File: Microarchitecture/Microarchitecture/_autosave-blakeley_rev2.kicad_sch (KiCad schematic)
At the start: 15 parts

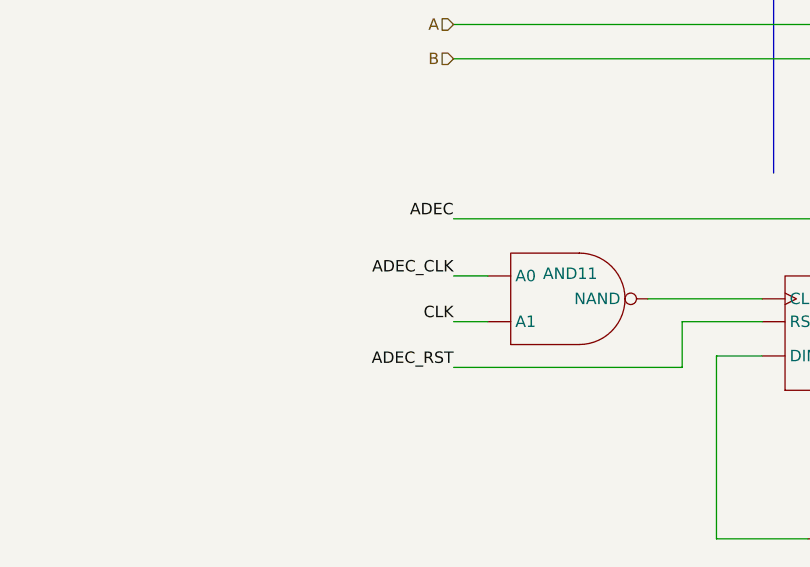
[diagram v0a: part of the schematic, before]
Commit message: Blakeley datapath working
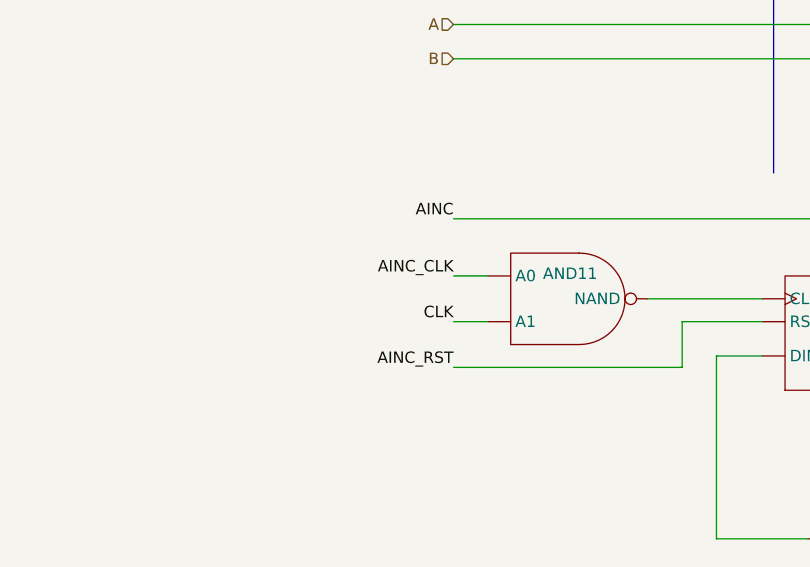
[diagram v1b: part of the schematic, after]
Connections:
- net ADEC_CLK is gone; now on net CLK: AND11. (NAND)
- net ADEC_RST is gone; now on net AINC_RST: REG29. (RST)
- net AINC_RST: now reaches REG29. (RST)
- net AINC_RST: no longer AND11. (NAND)
- net AINC: now reaches ADD16. (DIN1[log2(W)-1...0]), REG29. (RST)
- net AINC: now also DECODE7. (D[W-1...0])
- removed net ADEC: ADD16. (DIN1[log2(W)-1...0]), DECODE7. (D[W-1...0]), REG29. (RST)
- new net: MUX11. (MUX[W-1...0]), SUB12. (SUB[W-1...0])
- new net: AND12. (AND), REG31. (RST)
- new net: MUX11. (MUX[W-1...0]), REG31. (RST)
- new net: 3AND14. (AND3), 3AND15. (AND3), 3ANDW5. (AND3), ADD17. (DIN1[W-1...0])
- new net: 3AND14. (AND3), 3AND15. (AND3), 3ANDW5. (AND3), DECODE7. (D[W-1...0])
- new net: MUX11. (MUX[W-1...0]), SUB8. (SUB[W-1...0])
- new net: ADD17. (DIN1[W-1...0]), SHIFT9. (DOUT[W-1...0])
- new net: AND11. (NAND), REG29. (RST)
- new net: ADD16. (DIN1[log2(W)-1...0]), REG29. (RST)
- new net AINC_CLK: AND11. (NAND)
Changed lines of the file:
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@@
 		)
 	)
-	(label "ADEC_RST"
+	(label "AINC_RST"
 		(at 119.38 96.52 180)
 		(fields_autoplaced yes)
@@
 		)
 	)
-	(label "ADEC"
+	(label "AINC"
 		(at 119.38 80.01 180)
 		(fields_autoplaced yes)
@@
 		)
 	)
-	(label "ADEC_CLK"
+	(label "AINC_CLK"
 		(at 119.38 86.36 180)
 		(fields_autoplaced yes)

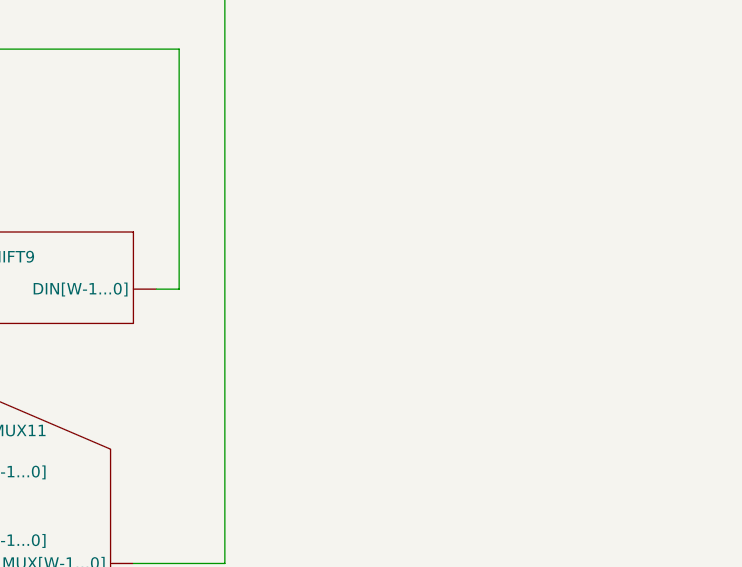
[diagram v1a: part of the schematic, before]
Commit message: Both datapath and ctl working independently
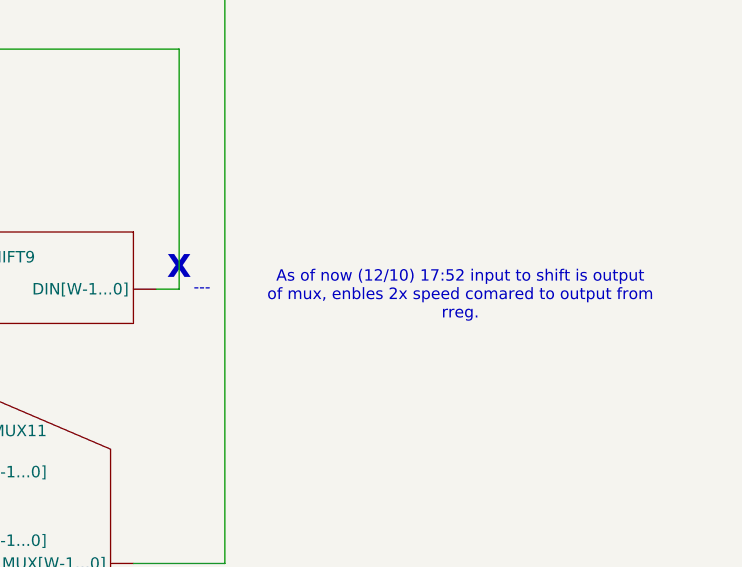
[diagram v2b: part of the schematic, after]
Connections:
- new net: MUX11. (MUX[W-1...0]), SUB12. (SUB[W-1...0])
- new net: AND12. (AND), REG31. (RST)
- new net: MUX11. (MUX[W-1...0]), REG31. (RST)
- new net: 3AND14. (AND3), 3AND15. (AND3), 3ANDW5. (AND3), ADD17. (DIN1[W-1...0])
- new net: 3AND14. (AND3), 3AND15. (AND3), 3ANDW5. (AND3), DECODE7. (D[W-1...0])
- new net: MUX11. (MUX[W-1...0]), SUB8. (SUB[W-1...0])
- new net: ADD17. (DIN1[W-1...0]), SHIFT9. (DOUT[W-1...0])
- new net: AND11. (NAND), REG29. (RST)
- new net: ADD16. (DIN1[log2(W)-1...0]), REG29. (RST)
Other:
- note added: "---"
- note added: "As of now (12/10) 17:52 input to shift is output of mux, enbles 2x speed comared to output from rreg."
- note added: "X"
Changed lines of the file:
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@@
+		)
+	)
+	(text "As of now (12/10) 17:52 input to shift is output\nof mux, enbles 2x speed comared to output from\nrreg."
+		(exclude_from_sim no)
+		(at 362.712 134.112 0)
+		(effects
+			(font
+				(size 1.27 1.27)
+			)
+		)
+	)
+	(text "X"
+		(exclude_from_sim no)
+		(at 331.47 131.064 0)
+		(effects
+			(font
+				(size 2.54 2.54)
+				(thickness 0.508)
+				(bold yes)
+			)
 		)
 	)
@@
 		(effects
 			(font
+				(size 1.27 1.27)
+			)
+		)
+	)
+	(text "---"
+		(exclude_from_sim no)
+		(at 334.01 133.35 0)
+		(effects
+			(font

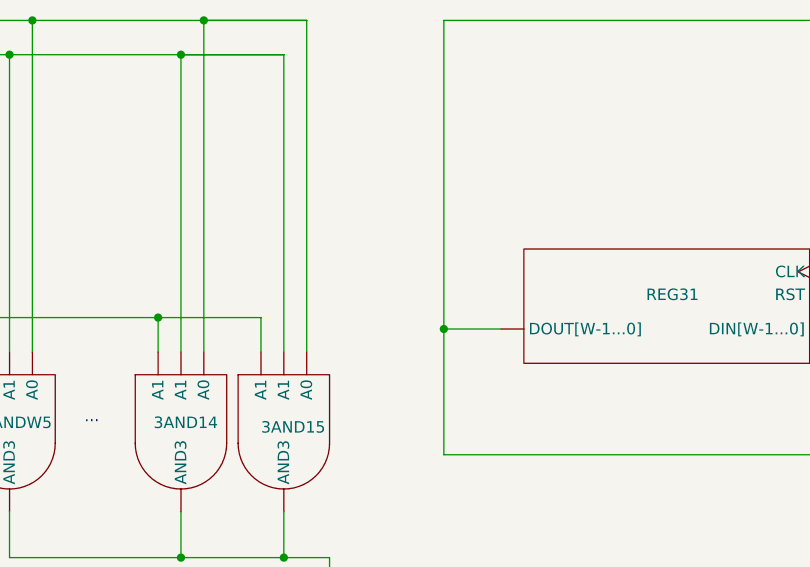
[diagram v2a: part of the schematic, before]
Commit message: TB for blakeley module ok, discovered datapath add logic error
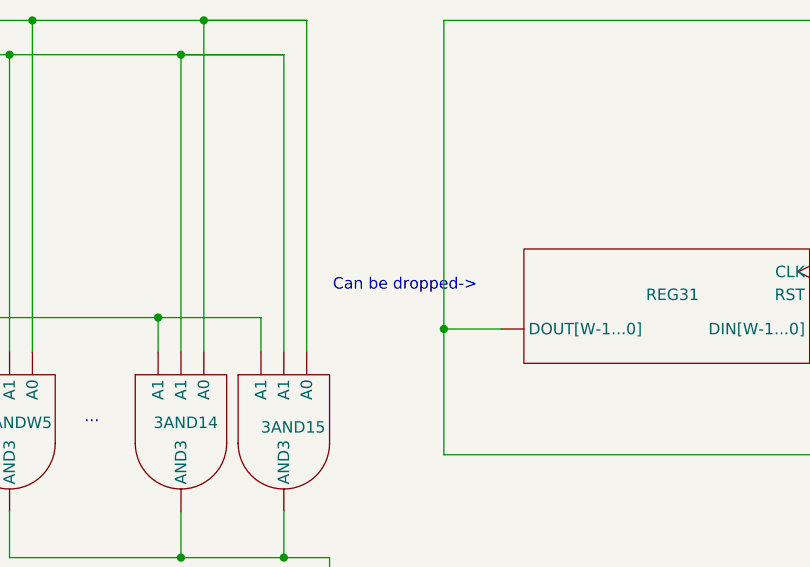
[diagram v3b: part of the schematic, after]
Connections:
- new net: MUX11. (MUX[W-1...0]), SUB12. (SUB[W-1...0])
- new net: AND12. (AND), REG31. (RST)
- new net: MUX11. (MUX[W-1...0]), REG31. (RST)
- new net: 3AND14. (AND3), 3AND15. (AND3), 3ANDW5. (AND3), ADD17. (DIN1[W-1...0])
- new net: 3AND14. (AND3), 3AND15. (AND3), 3ANDW5. (AND3), DECODE7. (D[W-1...0])
- new net: MUX11. (MUX[W-1...0]), SUB8. (SUB[W-1...0])
- new net: ADD17. (DIN1[W-1...0]), SHIFT9. (DOUT[W-1...0])
- new net: AND11. (NAND), REG29. (RST)
- new net: ADD16. (DIN1[log2(W)-1...0]), REG29. (RST)
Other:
- note added: "Can be dropped->"
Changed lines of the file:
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@@
+		)
+	)
+	(text "Can be dropped->\n"
+		(exclude_from_sim no)
+		(at 285.242 87.884 0)
+		(effects
+			(font
+				(size 1.27 1.27)
+			)
 		)
 	)
